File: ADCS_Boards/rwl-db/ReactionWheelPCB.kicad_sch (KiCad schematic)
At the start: 35 parts, among them J1 PC104_Connector, J2 Conn_02x11_Odd_Even, J3 Conn_02x11_Odd_Even, J4 Conn_02x11_Odd_Even, J5 Conn_02x11_Odd_Even, U1 Controller 1, U2 Controller 2, U3 Controller 3, U4 Controller 4, U5 LM358, U6 LM358

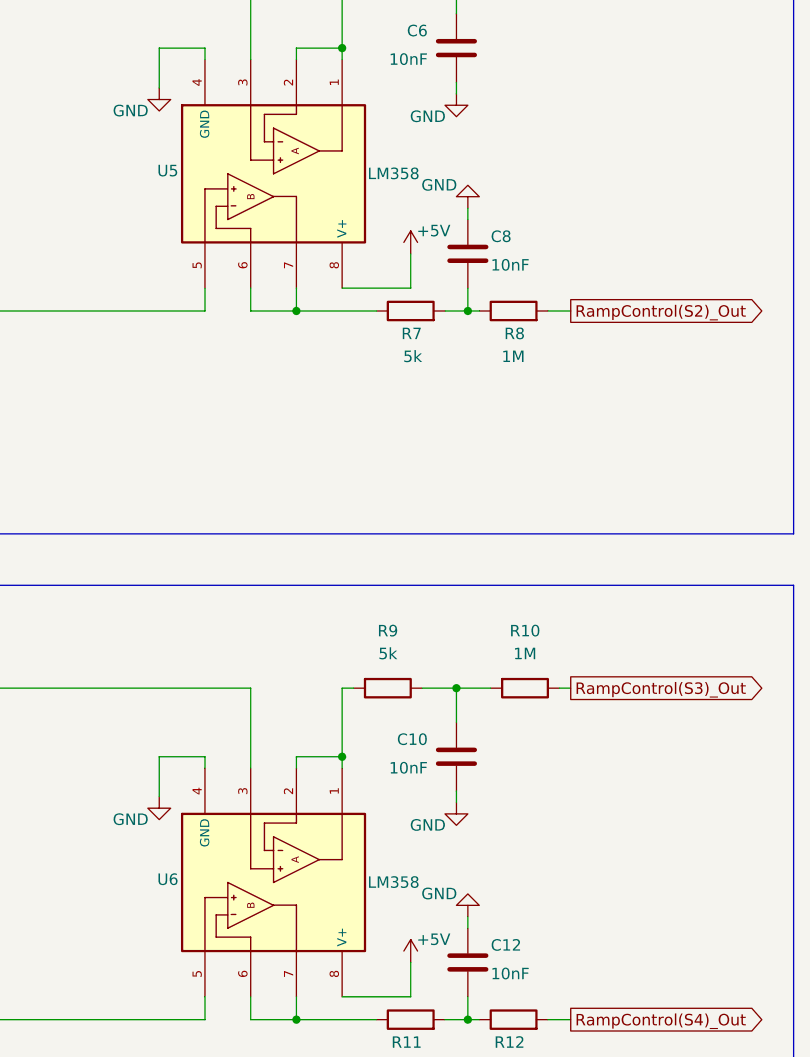
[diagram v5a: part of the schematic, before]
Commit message: adcs: rwl-db: updated 5k resistors to use 0402
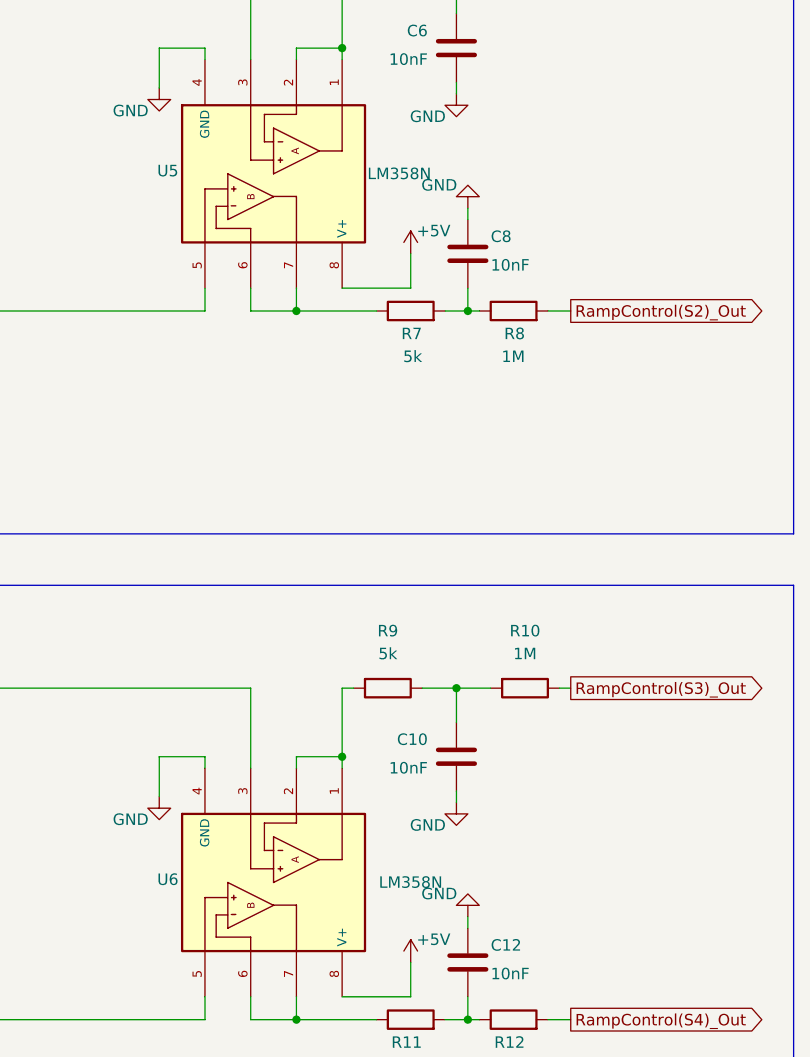
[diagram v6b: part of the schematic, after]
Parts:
- U5, U6: value LM358 -> LM358N
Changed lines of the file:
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@@
     (in_bom yes) (on_board yes)
     (property "Reference" "U6" (id 0) (at 72.0725 206.6925 90))
-    (property "Value" "LM358" (id 1) (at 97.155 207.01 90))
+    (property "Value" "LM358N" (id 1) (at 99.06 207.01 90))
     (property "Footprint" "qset-footprints:DIP794W45P254L959H508Q8" (id 2) (at 72.39 207.01 0)
       (effects (font (size 1.27 1.27)) hide)
@@
     (in_bom yes) (on_board yes)
     (property "Reference" "U5" (id 0) (at 72.0725 127.9525 90))
-    (property "Value" "LM358" (id 1) (at 97.155 128.27 90))
+    (property "Value" "LM358N" (id 1) (at 97.79 128.27 90))
     (property "Footprint" "qset-footprints:DIP794W45P254L959H508Q8" (id 2) (at 72.39 128.27 0)
       (effects (font (size 1.27 1.27)) hide)
@@
     )
     (path "/f779d80d-76c7-417d-b22f-8391e145bedd"
-      (reference "U5") (unit 1) (value "LM358") (footprint "qset-footprints:DIP794W45P254L959H508Q8")
+      (reference "U5") (unit 1) (value "LM358N") (footprint "qset-footprints:DIP794W45P254L959H508Q8")
     )
     (path "/a91ac937-6db0-4544-a6d5-2fc696e30a86"
-      (reference "U6") (unit 1) (value "LM358") (footprint "qset-footprints:DIP794W45P254L959H508Q8")
-    )
-  )
+      (reference "U6") (unit 1) (value "LM358N") (footprint "qset-footprints:DIP794W45P254L959H508Q8")
+    )
+  )
